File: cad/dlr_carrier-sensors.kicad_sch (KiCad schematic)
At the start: 15 parts, among them J10 YL-83, J8 FLIR_LEPTON_FFC, J9 SI1145, U5 DHT22, U6 ADS1115

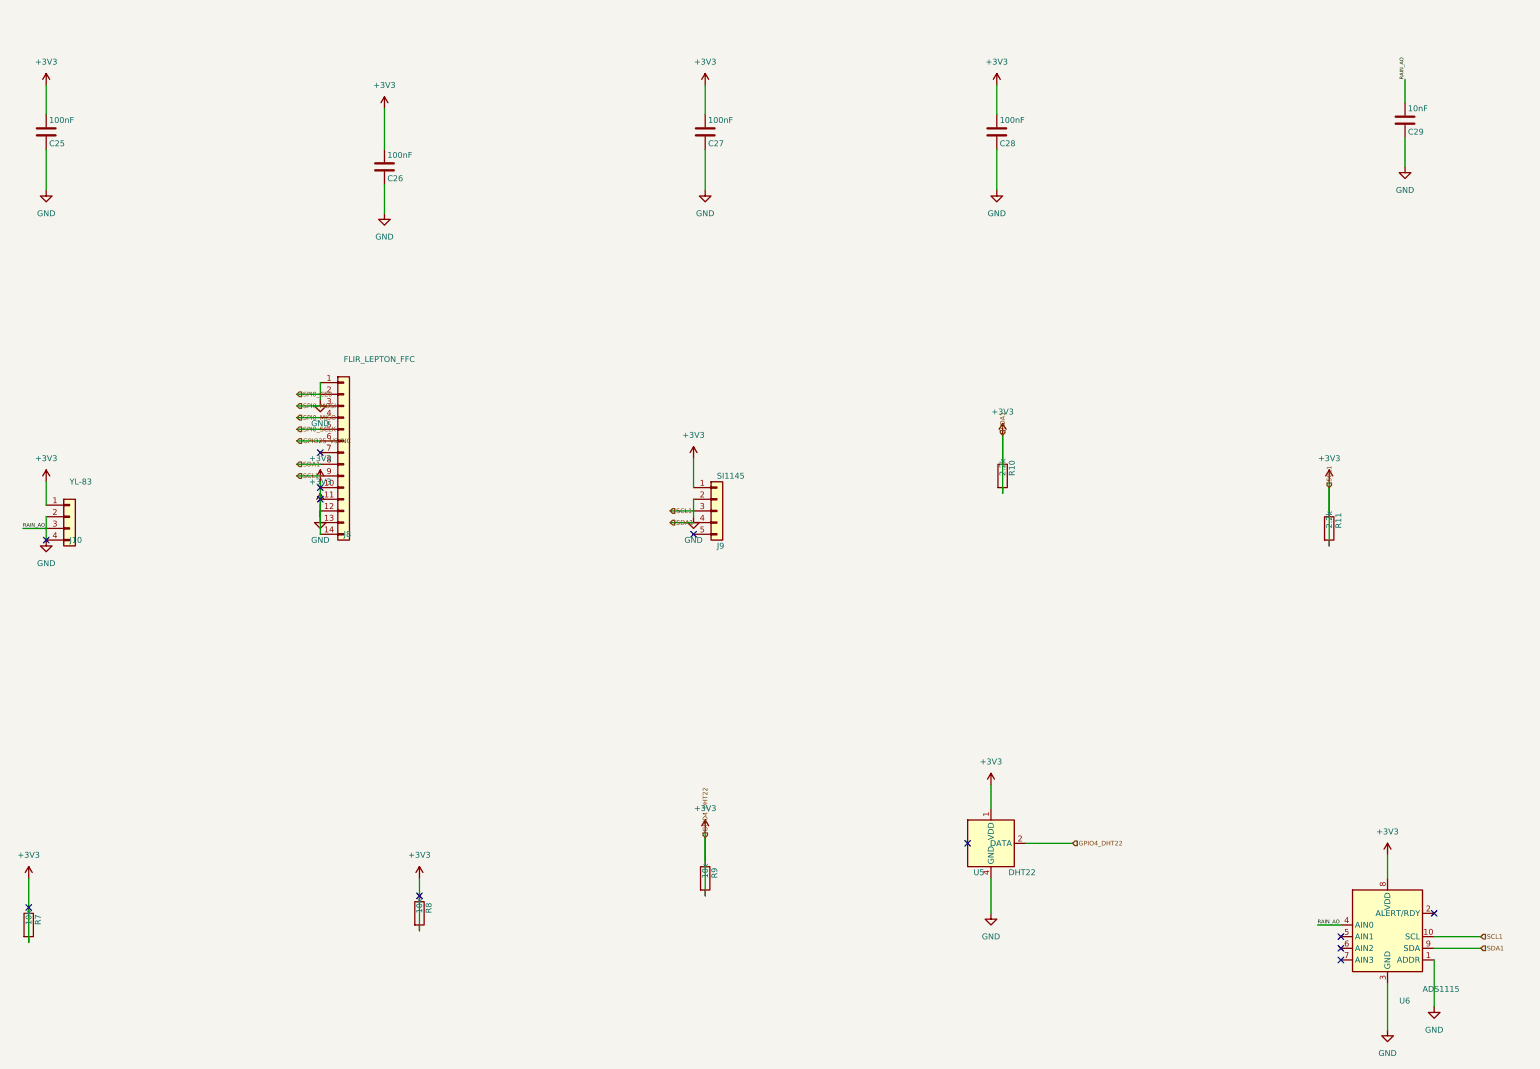
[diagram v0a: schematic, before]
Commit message: 🎨 style: lint fixes (f-string, unused imports, complexity, naming)
CI lint surface from the prior commit:
* F541: drop extraneous `f` prefixes on f-strings without placeholders
* F401: remove unused `math` and `_place_pwr_flags` imports
* C901: extract `_route_sheet_nets` helper so `build_child_sheet`
  complexity drops back under the McCabe threshold
* N806: lowercase local constants in `build_root_sheet`
* black: reformat multi_sheet.py + schematic.py

Co-Authored-By: Claude Opus 4.7 (1M context) <noreply@anthropic.com>
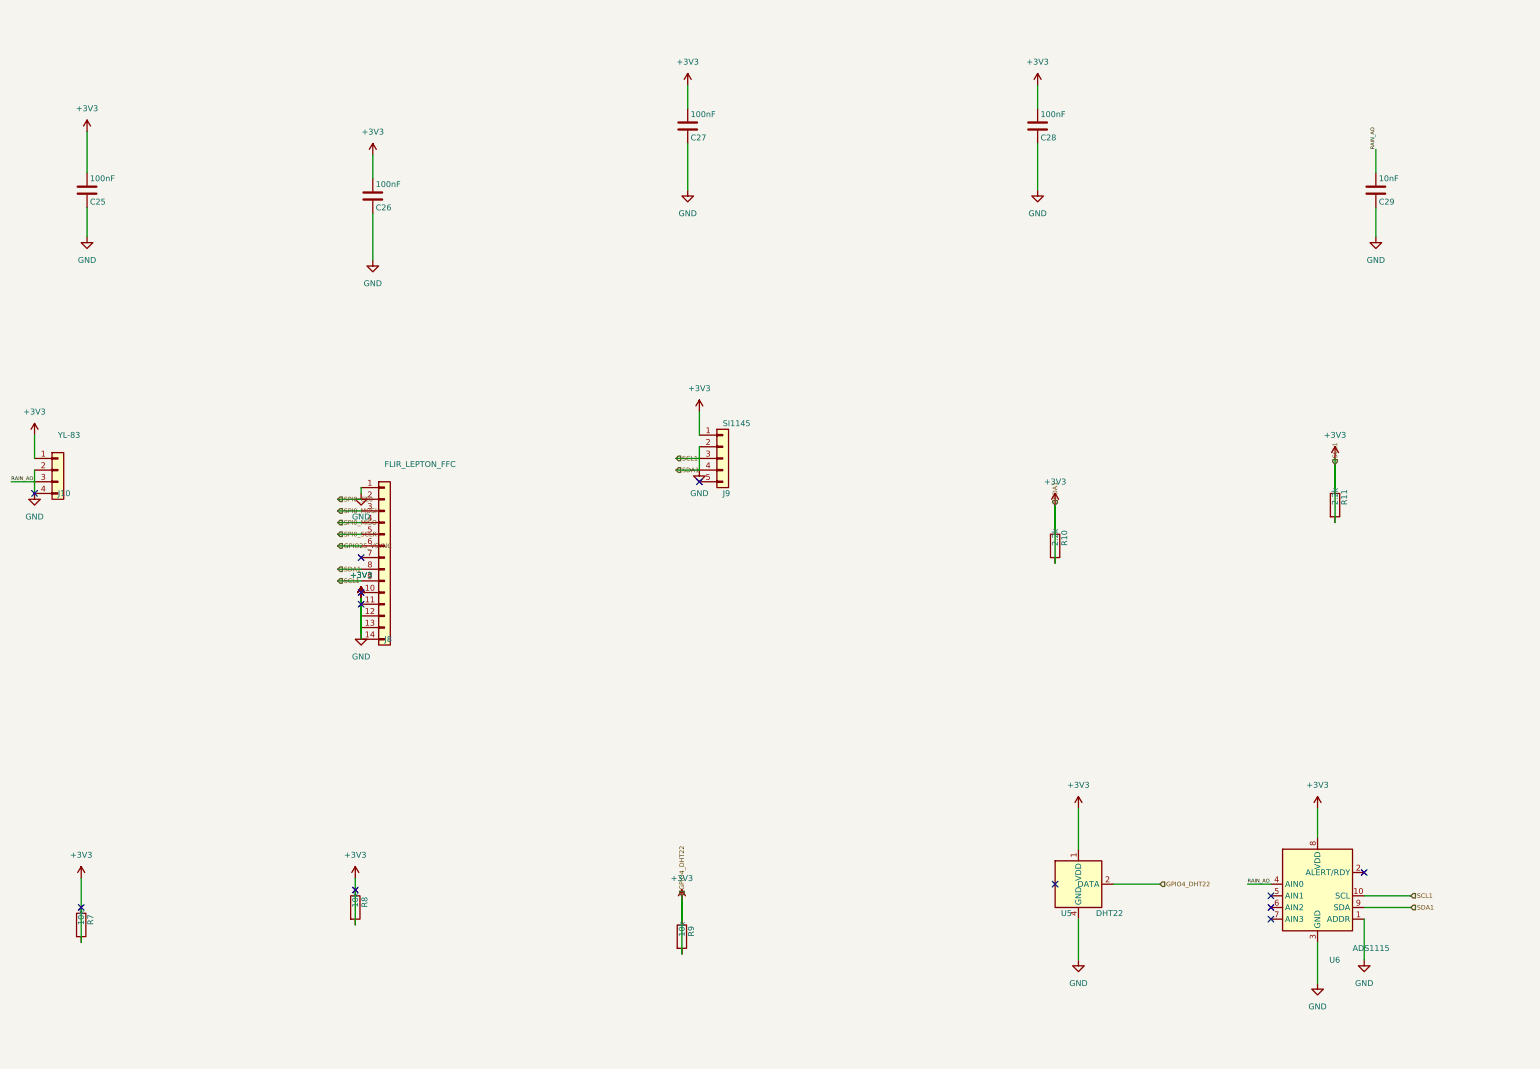
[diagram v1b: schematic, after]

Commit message: 🪪 feat(anemometer): low-wind variant — Vaisala WMT702, kit SKU split
Locks the low-wind variant per the grill-me design tree. Single PCB +
single firmware binary; the variant lives in the kit BOM (sensor + cable
harness + PV panel + battery). Both sensors speak NMEA 0183 over the
RS-485 transceiver so the driver is talker-agnostic.

Hardware:
* anemometer.py: add SMBJ24CA TVS on V+→GND for IEC 61000-4-5 2 kV
  surge tolerance (utility-tower deployment).

Theory:
* theory.ipynb §6: variant-aware power-budget cell. WMT702's 480 mW
  draw needs a 30 W panel + 100 Wh battery to hold 1.66× winter margin
  and 2.22 d autonomy. High-wind kit (Calypso, 1 mW) stays on the
  existing 20 W / 50 Wh baseline.
* Expected-values table rebuilt with per-variant rows.

README:
* New "Anemometer Variants" section: full kit BOM table, deployment
  decision rule (NREL WIND Toolkit climatology, 15 % yr V_w<1 m/s
  threshold), fallback policy, per-variant power numbers.

Co-Authored-By: Claude Opus 4.7 (1M context) <noreply@anthropic.com>
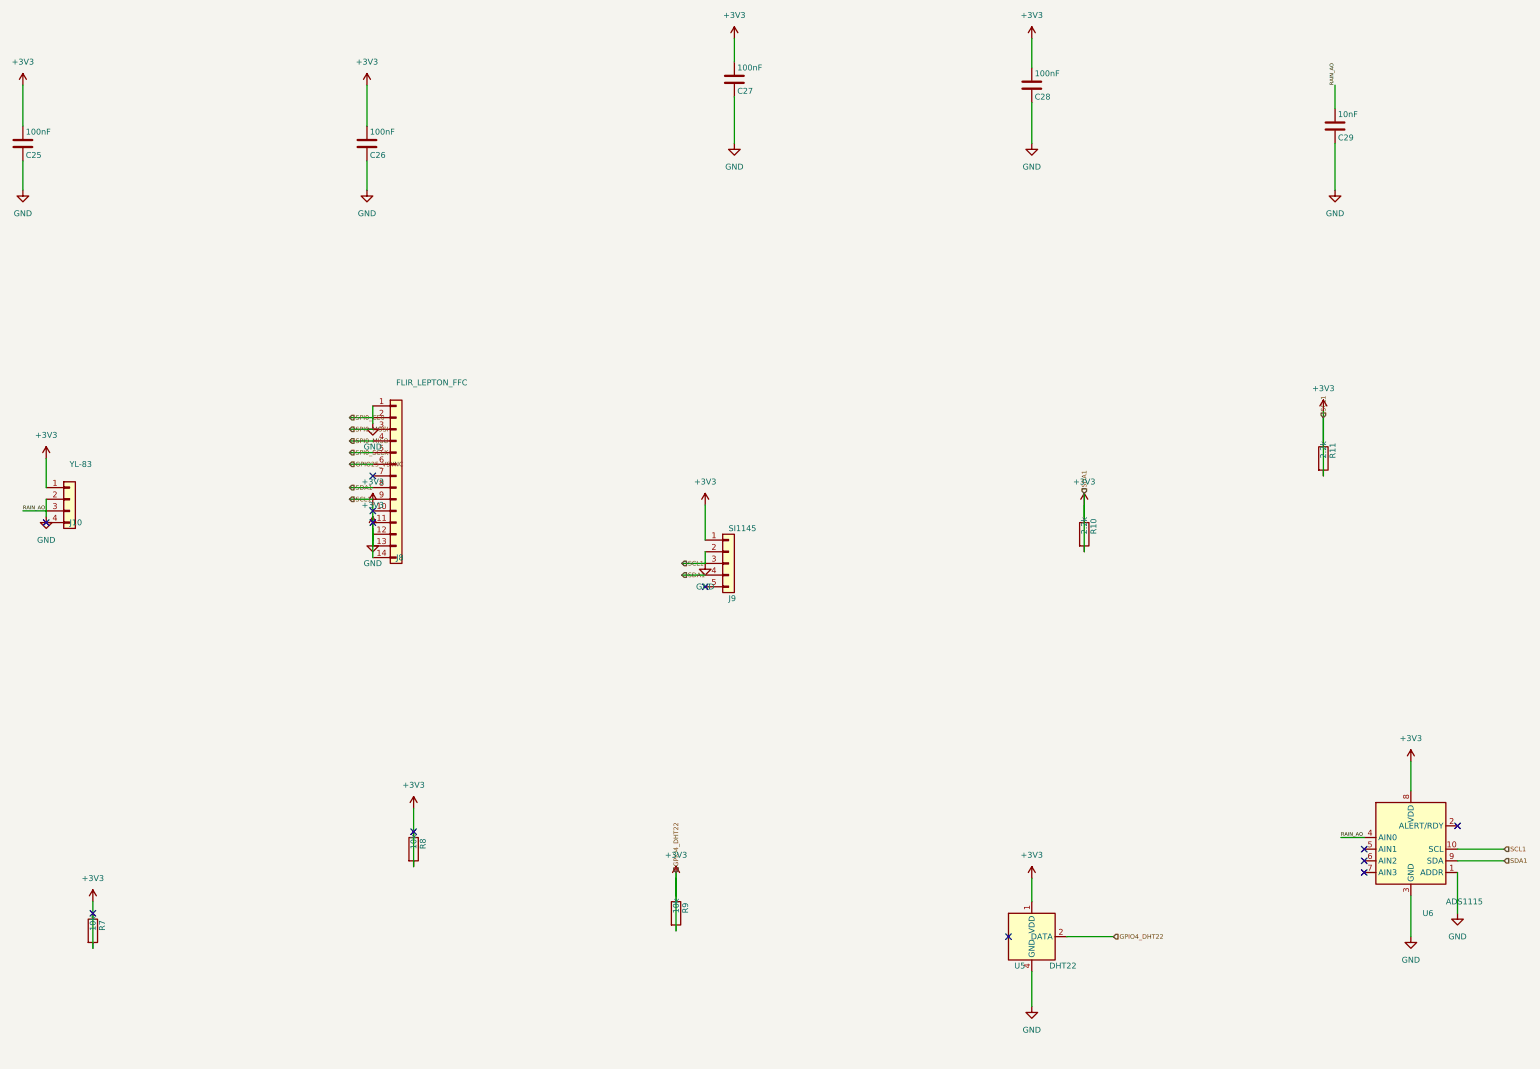
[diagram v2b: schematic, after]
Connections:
- net +3V3: no longer J10.4 (Pin_4)
